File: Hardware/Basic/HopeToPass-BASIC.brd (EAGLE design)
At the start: 38 x 38 mm, 52 parts, among them SW1 SWITCH.MOM, SW2 SWITCH.MOM, SW5 SWITCH.MOM, U2 NRF52832_MODULE_MDBT42, U4 PCF8523

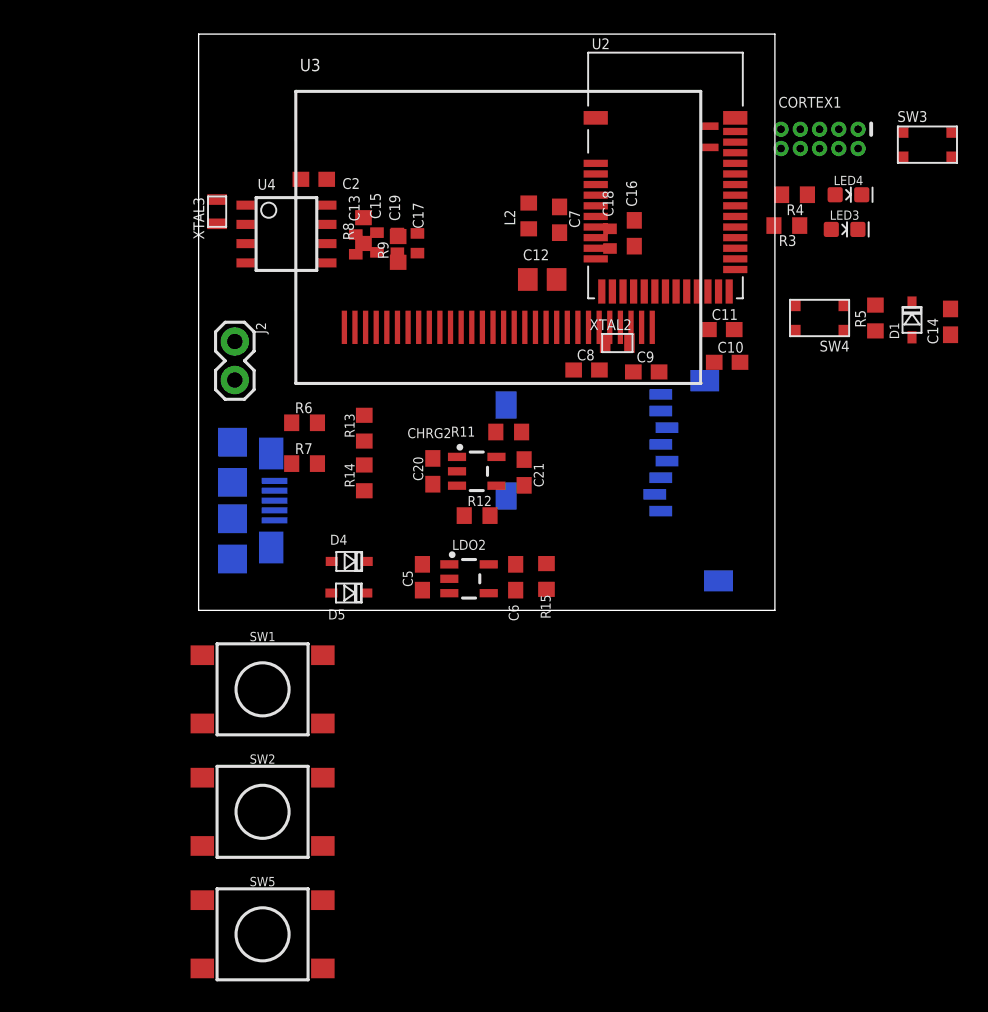
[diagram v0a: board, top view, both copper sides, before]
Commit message: Complete eagle 001 and started programming
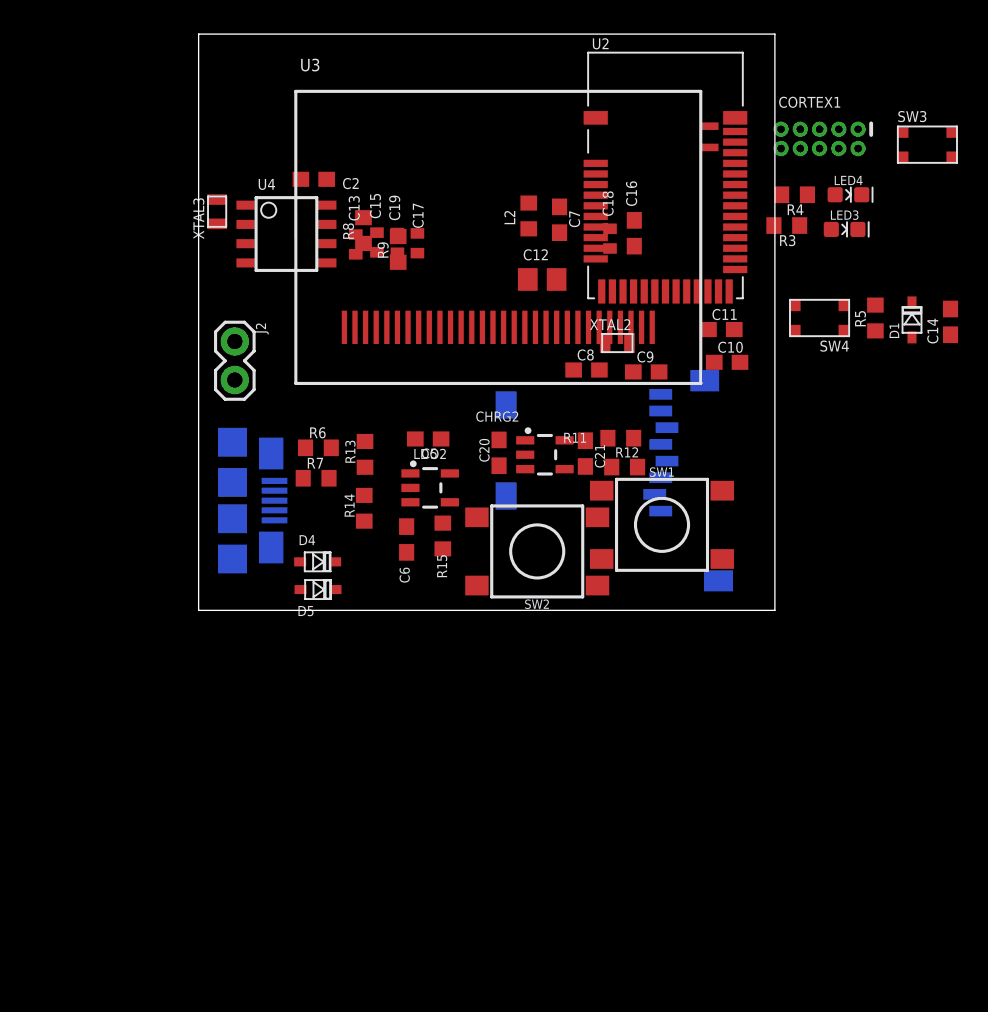
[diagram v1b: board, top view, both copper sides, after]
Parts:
- removed SW5: SWITCH.MOM, LinnesLab-Switches:TACTILE_SWITCH_SMD_6.2MM_TALL
- moved SW1 28.5 mm to (30.6, 5.64)
- moved SW2 25.0 mm to (22.3, 3.89), turned to 180 degrees
- moved R12 10.2 mm to (28.1, 9.45)
- moved C5 9.13 mm to (15.1, 11.3), turned to 180 degrees
- moved C6 7.61 mm to (13.7, 4.67)
- moved R11 7.40 mm to (27.8, 11.4)
- moved R15 7.33 mm to (16.1, 4.90)
- moved LDO2 6.52 mm to (15.3, 8.08)
- moved CHRG2 4.63 mm to (22.8, 10.3)
- moved C20 4.54 mm to (19.8, 10.4)
- moved C21 4.23 mm to (25.5, 10.3)
- moved D4 2.08 mm to (7.85, 3.20)
- moved D5 2.04 mm to (7.87, 1.37)
- moved R14 2.01 mm to (10.9, 6.73)
- moved R6 1.89 mm to (7.90, 10.7)
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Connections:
- net VBATT renamed VBAT
- removed net N$21: SW1.B1, SW1.B2
- removed net N$22: SW1.A1
- new net SW1: SW1.A1, SW2.A1
- net GND: now also SW1.B1, SW1.B2, SW2.B1, SW2.B2

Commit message: 10/16 updates
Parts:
- removed C2: 1u, LinnesLab-Passives:C0603
- removed SD2: (no value), LinnesLab-Connectors:MICROSD
- removed U4: PCF8523, LinnesLab-Clocks:SO8
- removed USB2: USB.MICRO-BIGGERPADS, LinnesLab-Connectors:USB-MICRO-01.BIGGERPADS
- removed XTAL3: 32.7680kHz, LinnesLab-Clocks:2-SMD.NOLEAD.2.0MMTO1.2MM
- added C3: 1u, LinnesLab-Passives:C0603
- added J1: FTDI_DEVICESMD, LinnesLab-Connectors:FTDI-SMD
- added J3: (no value), LinnesLab-Connectors:1X07_1.27MM
- added U5: PCF8523, LinnesLab-Clocks:SO8
- added XTAL4: 32.7680kHz, LinnesLab-Clocks:2-SMD.NOLEAD.2.0MMTO1.2MM
- C13, C15, C17, C18, C19: device LinnesLab-Passives:C0402 -> LinnesLab-Passives:C0603
- moved R11 34.7 mm to (-6.81, 10.6)
- moved C20 21.3 mm to (4.95, -4.90)
- moved R7 21.3 mm to (15.1, 28.7), turned to 90 degrees
- moved R13 19.6 mm to (-0.97, -5.31)
- moved R12 19.6 mm to (8.89, 5.49), turned to 180 degrees
- moved C21 19.5 mm to (6.17, 7.98), turned to 90 degrees
- moved C14 18.2 mm to (34.3, 9.14), turned to 0 degrees
- moved R14 17.5 mm to (-6.32, 3.91)
- moved SW3 14.7 mm to (34.2, 35.6), turned to 180 degrees
- moved D1 14.7 mm to (34.4, 11.7), turned to 180 degrees
- moved CHRG2 14.1 mm to (8.97, 7.95), turned to 90 degrees
- moved C9 14.1 mm to (16.9, 21.9), turned to 90 degrees
- moved R9 13.9 mm to (3.35, 33.6)
- moved R6 12.8 mm to (13.7, 22.1), turned to 270 degrees
- moved C12 12.6 mm to (13.3, 30.3), turned to 268.7 degrees
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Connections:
- net CHRG.STAT renamed D27/CHRG.STAT
- removed net BATT: R13.1, R14.2
- removed net CD1: SD2.CD1
- removed net CD2: SD2.CD2
- removed net CS.OLED: U3.13
- removed net DC.OLED: U3.15
- removed net N$19: U4.2, XTAL3.P$1
- removed net N$20: U4.1, XTAL3.P$2
- removed net RESET.OLED: U3.14
- removed net RXD: U2.21
- removed net SD.CS: SD2.2
- removed net SW1: SW1.A1, SW2.A1
- removed net TXD: U2.19
- removed net USB+: USB2.3
- removed net USB-: USB2.2
- removed net VBAT: U4.3
- new net A4/PPG: J3.7, U2.5
- new net A5/TIA: J3.6, U2.6
- new net A7/BATT: R13.1, R14.2, U2.8
- new net D11/SW1: SW1.A1, U2.25
- new net D15/SW2: SW2.A1, U2.29
- new net D16/CS.OLED: U2.30, U3.13
- new net D27/CHRG.STATUS: U2.4
- new net D3/RESET.OLED: U2.16, U3.14
- new net D30/LED.CTRL: J3.5, U2.7
- new net D4/DC.OLED: U2.17, U3.15
- new net D5/CD1: U2.18
- new net D7/SD.CS: U2.20
- new net N$21: U5.2, XTAL4.P$1
- new net N$22: U5.1, XTAL4.P$2
- new net RXD.NRF: J1.TXO, U2.21
- new net TXD.NRF: J1.RXI, U2.19
- new net VBATT: U5.3
- net 3.3V: now also C3.1, J3.4, U5.8; no longer C2.1, SD2.4, U4.8
- net DTR: now also J1.DTR
- net GND: now also C3.2, J1.CTS, J1.GND, J3.3, U5.4; no longer C2.2, SD2.6, SD2.MT1, SD2.MT2, U4.4, USB2.5
- net MISO: no longer SD2.7
- net MOSI: no longer SD2.3
- net SCK: no longer SD2.5
- net SCL: now also J3.2, U5.6; no longer U4.6
- net SDA: now also J3.1, U5.5; no longer U4.5
- net V_USB: now also J1.VCC; no longer USB2.1
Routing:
- net GND: track 0.00 -> 33.9 mm, vias 0 -> 17
- net RESET: track 0.00 -> 30.3 mm, vias 0 -> 1
- net V_USB: track 0.00 -> 13.0 mm, vias 0 -> 1
- net DFU: track 0.00 -> 12.1 mm, vias 0 -> 2
- net VIN: track 0.00 -> 12.1 mm
- net SWCLK: track 0.00 -> 9.88 mm, vias 0 -> 1
- net SDA: track 0.00 -> 9.10 mm
- net SWO: track 0.00 -> 8.71 mm, vias 0 -> 1
- net N$4: track 0.00 -> 8.69 mm
- net 3.3V: track 0.00 -> 7.77 mm
- net N$6: track 0.00 -> 7.68 mm
- net SCL: track 0.00 -> 7.30 mm
- net SWDIO: track 0.00 -> 5.90 mm
- net LED2: track 0.00 -> 5.80 mm
- net N$5: track 0.00 -> 5.32 mm
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- added copper zone on layer 1, net 3.3V
- added copper zone on layer 16, net GND

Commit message: Completed Routing the board
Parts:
- removed C10, C11: 300p, LinnesLab-Passives:C0603
- removed R15: 100k, LinnesLab-Passives:R0603
- moved R13 26.3 mm to (3.53, 20.6), turned to 270 degrees
- moved C18 19.2 mm to (32.3, 18.2), turned to 90 degrees
- moved R7 18.9 mm to (30.9, 18.2), turned to 270 degrees
- moved R14 18.6 mm to (1.80, 20.6)
- moved R11 17.2 mm to (8.13, 1.96), turned to 0 degrees
- moved C16 15.6 mm to (29.3, 18.2), turned to 90 degrees
- moved C20 14.1 mm to (9.53, 8.46), turned to 180 degrees
- moved C12 4.73 mm to (18.0, 30.4), turned to 358.7 degrees
- moved C7 2.69 mm to (18.0, 28.5), turned to 180 degrees
- moved L2 2.20 mm to (18.0, 26.7), turned to 0 degrees
- moved R12 2.06 mm to (9.04, 3.43)
- moved C21 2.01 mm to (6.15, 5.97)
- moved CHRG2 1.91 mm to (9.02, 6.05)
- moved J2 1.09 mm to (2.54, 17.5)
- moved D4 0.54 mm to (2.11, 11.2)
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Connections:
- removed net D27/CHRG.STAT: CHRG2.1, R12.1
- removed net P0.09/NFC1: C11.1, U2.22
- removed net P0.10/NFC2: C10.1, U2.23
- net 3.3V: no longer R15.2
- net D27/CHRG.STATUS: now also CHRG2.1, R12.1
- net GND: no longer C10.2, C11.2, R15.1, SW1.B2, SW2.B2
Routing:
- net D27/CHRG.STATUS: track 0.00 -> 38.2 mm, vias 0 -> 4
- net GND: track 33.9 -> 63.9 mm, vias 17 -> 42
- net A7/BATT: track 0.00 -> 26.5 mm
- net TXD.NRF: track 0.00 -> 25.6 mm, vias 0 -> 1
- net SCL: track 7.30 -> 31.8 mm
- net DTR: track 0.00 -> 22.3 mm, vias 0 -> 1
- net SDA: track 9.10 -> 31.3 mm, vias 0 -> 1
- net D15/SW2: track 0.00 -> 21.8 mm, vias 0 -> 2
- net D11/SW1: track 0.00 -> 21.4 mm, vias 0 -> 2
- net RXD.NRF: track 0.00 -> 20.1 mm, vias 0 -> 1
- net D16/CS.OLED: track 0.00 -> 19.5 mm, vias 0 -> 2
- net SCK: track 0.00 -> 18.0 mm, vias 0 -> 2
- net VLIPO: track 2.18 -> 20.2 mm
- net MOSI: track 0.00 -> 17.7 mm, vias 0 -> 2
- net D30/LED.CTRL: track 0.00 -> 15.1 mm, vias 0 -> 1
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
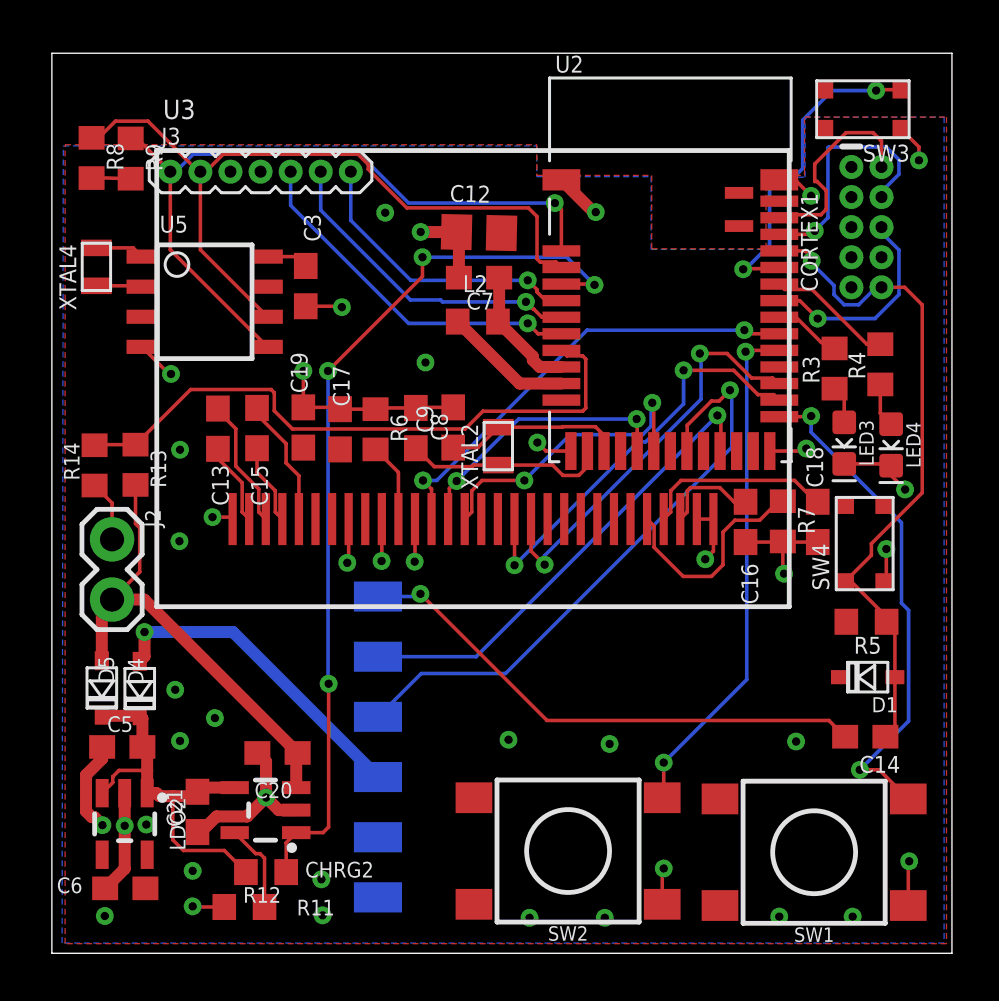
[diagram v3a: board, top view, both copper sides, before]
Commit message: orlando renumbered components
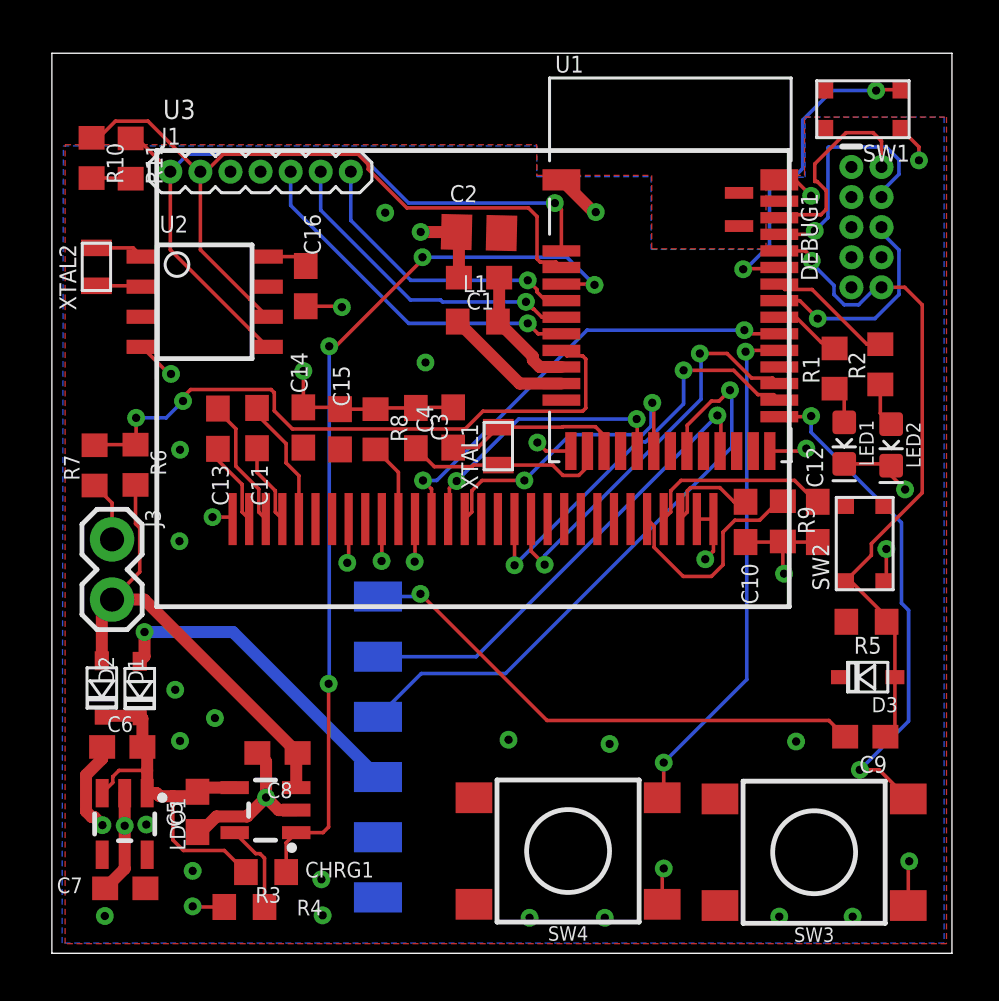
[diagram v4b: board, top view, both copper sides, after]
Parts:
- removed C17, C18, C19: 2.2uF, LinnesLab-Passives:C0603
- removed C20, C21: 4.7u, LinnesLab-Passives:C0603
- removed D4: (no value), LinnesLab-DiscreteSemi:USC
- removed R12, R13, R14: 100k, LinnesLab-Passives:R0603
- removed U5: PCF8523, LinnesLab-Clocks:SO8
- removed XTAL4: 32.7680kHz, LinnesLab-Clocks:2-SMD.NOLEAD.2.0MMTO1.2MM
- added C1: 1u, LinnesLab-Passives:C0603
- added C10: 10uF, LinnesLab-Passives:C0603
- added C11: 2.2uF, LinnesLab-Passives:C0603
- added C2: 10u, LinnesLab-Passives:C0805
- added C4: 22p, LinnesLab-Passives:C0603
- added D3: (no value), LinnesLab-DiscreteSemi:USC
- added R1, R2: 1k, LinnesLab-Passives:R0603
- added R10: 10k, LinnesLab-Passives:R0603
- added U1: NRF52832_MODULE_MDBT42, LinnesLab-Microcontrollers:BLE_MODULE_RAYTAC_MDBT42
- added XTAL1: 32.768kHz, LinnesLab-Clocks:2-SMD.NOLEAD.2.0MMTO1.2MM
- C12: value 10u -> 2.2uF; device LinnesLab-Passives:C0805 -> LinnesLab-Passives:C0603
- C14: value 100n -> 2.2uF
- C16: value 10uF -> 1u
- C3: value 1u -> 22p
- C5: value 1u -> 4.7u
- C8: value (none) -> 4.7u
- C9: value (none) -> 100n
- J1: value FTDI_DEVICESMD -> (none); device LinnesLab-Connectors:FTDI-SMD -> LinnesLab-Connectors:1X07_1.27MM
- J2: value (none) -> FTDI_DEVICESMD; device LinnesLab-Connectors:1X02 -> LinnesLab-Connectors:FTDI-SMD
- J3: device LinnesLab-Connectors:1X07_1.27MM -> LinnesLab-Connectors:1X02
- R11: value (none) -> 10k
- R3: value 1k -> 100k
- R4: value 1k -> 4.7k
- R6: value 10k -> 100k
- R7: value 390k -> 100k
- R9: value 10k -> 390k
- SW1, SW2: value SWITCH.MOM -> (none); device LinnesLab-Switches:TACTILE_SWITCH_SMD_6.2MM_TALL -> LinnesLab-Switches:BUTTON-GULLWING
- SW3, SW4: value (none) -> SWITCH.MOM; device LinnesLab-Switches:BUTTON-GULLWING -> LinnesLab-Switches:TACTILE_SWITCH_SMD_6.2MM_TALL
- U2: value NRF52832_MODULE_MDBT42 -> PCF8523; device LinnesLab-Microcontrollers:BLE_MODULE_RAYTAC_MDBT42 -> LinnesLab-Clocks:SO8
- XTAL2: value 32.768kHz -> 32.7680kHz
- moved R4 35.3 mm to (8.13, 1.96), turned to 0 degrees
- moved D1 32.3 mm to (2.11, 11.2), turned to 270 degrees
- moved R3 32.1 mm to (9.04, 3.43), turned to 180 degrees
- moved R11 32.0 mm to (3.33, 33.6), turned to 270 degrees
- moved R9 31.5 mm to (30.9, 18.2)
- moved SW1 31.4 mm to (34.2, 35.6)
- moved SW3 31.4 mm to (32.2, 4.27)
- moved C7 29.8 mm to (3.10, 2.74)
- moved R7 29.2 mm to (1.80, 20.6), turned to 90 degrees
- moved C14 27.1 mm to (10.6, 22.2), turned to 270 degrees
- moved J1 25.8 mm to (5.00, 33.0), flipped to the top, turned to 0 degrees
- moved C9 21.8 mm to (34.3, 9.14), turned to 0 degrees
- moved C16 21.1 mm to (10.7, 28.2), turned to 270 degrees
- moved U2 19.7 mm to (6.45, 27.5)
- moved C12 18.8 mm to (32.3, 18.2), turned to 90 degrees
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- renumbered CHRG2 to CHRG1, CORTEX1 to DEBUG1, D5 to D2, L2 to L1, LDO2 to LDO1, LED3 to LED1, LED4 to LED2
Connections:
- net 3.3V: now also C14.2, C15.2, C16.1, C2.2, C7.1, D3.-, J1.4, R10.2, R11.2, U1.11, U2.8; no longer C12.2, C17.2, C19.2, C3.1, C6.1, D1.-, J3.4, R8.2, R9.2, U2.11, U5.8
- net A4/PPG: now also J1.7, U1.5; no longer J3.7, U2.5
- net A5/TIA: now also J1.6, U1.6; no longer J3.6, U2.6
- net A7/BATT: now also R6.1, R7.2, U1.8; no longer R13.1, R14.2, U2.8
- net D11/SW1: now also SW3.A1, U1.25; no longer SW1.A1, U2.25
- net D15/SW2: now also SW4.A1, U1.29; no longer SW2.A1, U2.29
- net D16/CS.OLED: now also U1.30; no longer U2.30
- net D27/CHRG.STATUS: now also R3.1, U1.4; no longer R12.1, U2.4
- net D3/RESET.OLED: now also U1.16; no longer U2.16
- net D30/LED.CTRL: now also J1.5, U1.7; no longer J3.5, U2.7
- net D4/DC.OLED: now also U1.17; no longer U2.17
- net D5/CD1: now also U1.18; no longer U2.18
- net D7/SD.CS: now also U1.20; no longer U2.20
- net DFU: now also SW1.3, U1.34; no longer SW3.3, U2.34
- net DTR: now also C9.1, J2.DTR; no longer C14.1, J1.DTR
- net FRST: now also U1.38; no longer U2.38
- net GND: now also C1.2, C10.1, C14.1, C15.1, C16.2, C2.1, C3.1, C4.2, C6.1, C8.2, J1.3, J2.CTS, J2.GND, J3.1, R4.1, R7.1, R8.1, R9.2, SW1.1, SW2.3, SW3.B1, SW4.B1, U1.1, U1.12, U1.24, U1.39, U2.4; no longer C16.1, C17.1, C18.1, C19.1, C20.2, C21.1, C3.2, C6.2, C8.1, C9.2, J1.CTS, J1.GND, J2.1, J3.3, R11.1, R14.1, R6.1, R7.2, SW1.B1, SW2.B1, SW3.1, SW4.3, U2.1, U2.12, U2.24, U2.39, U5.4
- net LED1: now also R1.2, U1.31; no longer R3.2, U2.31
- net LED2: now also R2.2, U1.33; no longer R4.2, U2.33
- net MISO: now also U1.28; no longer U2.28
- net MOSI: now also U1.27; no longer U2.27
- net N$1: now also R8.2; no longer R6.2
- net N$10: now also R2.1; no longer R4.1
- net N$11: now also U1.10; no longer U2.10
- net N$12: now also C1.1, U1.9; no longer C7.1, U2.9
- net N$13: now also C10.2; no longer C16.2
- net N$15: now also C12.2; no longer C18.2
- net N$17: now also R4.2; no longer R11.2
- net N$2: now also R9.1; no longer R7.1
- net N$21: now also U2.2, XTAL2.P$1; no longer U5.2, XTAL4.P$1
- net N$22: now also U2.1, XTAL2.P$2; no longer U5.1, XTAL4.P$2
- net N$4: now also C3.2, U1.13, XTAL1.P$1; no longer C8.2, U2.13, XTAL2.P$1
- net N$6: now also C4.1, U1.14, XTAL1.P$2; no longer C9.1, U2.14, XTAL2.P$2
- net N$7: now also C11.2; no longer C15.2
- net N$8: now also C11.1; no longer C15.1
- net N$9: now also R1.1; no longer R3.1
- net RESET: now also C9.2, D3.+, SW2.1, U1.35; no longer C14.2, D1.+, SW4.1, U2.35
- net RXD.NRF: now also J2.TXO, U1.21; no longer J1.TXO, U2.21
- net SCK: now also U1.26; no longer U2.26
- net SCL: now also J1.2, R10.1, U1.3, U2.6; no longer J3.2, R8.1, U2.3, U5.6
- net SDA: now also J1.1, R11.1, U1.2, U2.5; no longer J3.1, R9.1, U2.2, U5.5
- net SWCLK: now also U1.36; no longer U2.36
- net SWDIO: now also U1.37; no longer U2.37
- net SWO: now also U1.32; no longer U2.32
- net TXD.NRF: now also J2.RXI, U1.19; no longer J1.RXI, U2.19
- net VBATT: now also U2.3; no longer U5.3
- net VIN: now also C6.2, D1.-, R3.2; no longer C21.2, D4.-, R12.2
- net VLIPO: now also C8.1, D1.+, J3.2, R6.2; no longer C20.1, D4.+, J2.2, R13.2
- net V_USB: now also J2.VCC; no longer J1.VCC
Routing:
- net A7/BATT: track 26.5 -> 27.2 mm, vias 0 -> 2
